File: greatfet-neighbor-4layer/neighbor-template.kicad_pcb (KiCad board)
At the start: 4 copper layers, 70.7 x 53.3 mm, 13 parts, among them J1 NEIGHBOR1, J2 NEIGHBOR2, J7 BONUS_ROW, U1 M24C02-FMN6TP

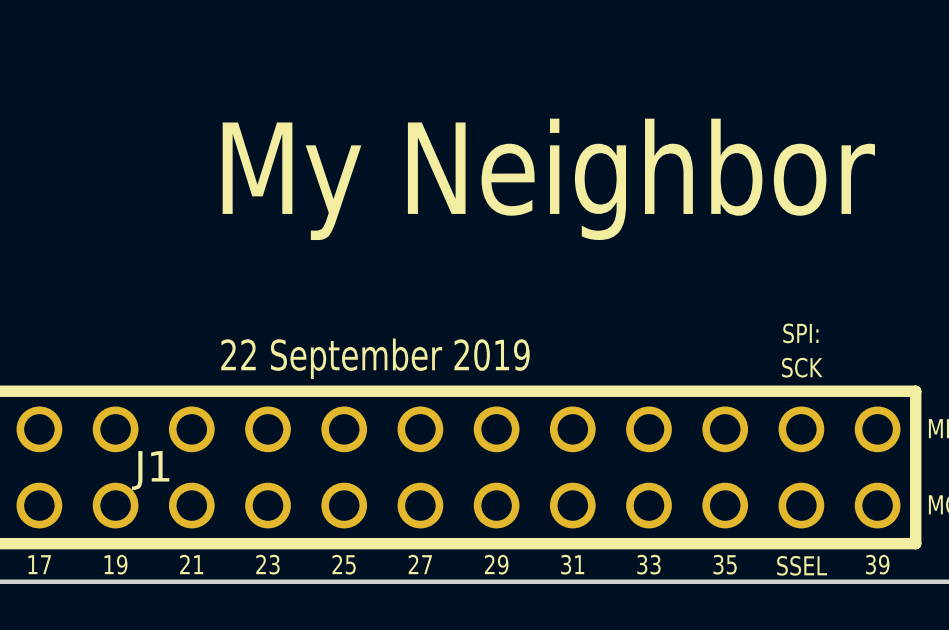
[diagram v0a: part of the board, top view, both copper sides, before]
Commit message: add "for GreatFET" to schematic, silkscreen add template README
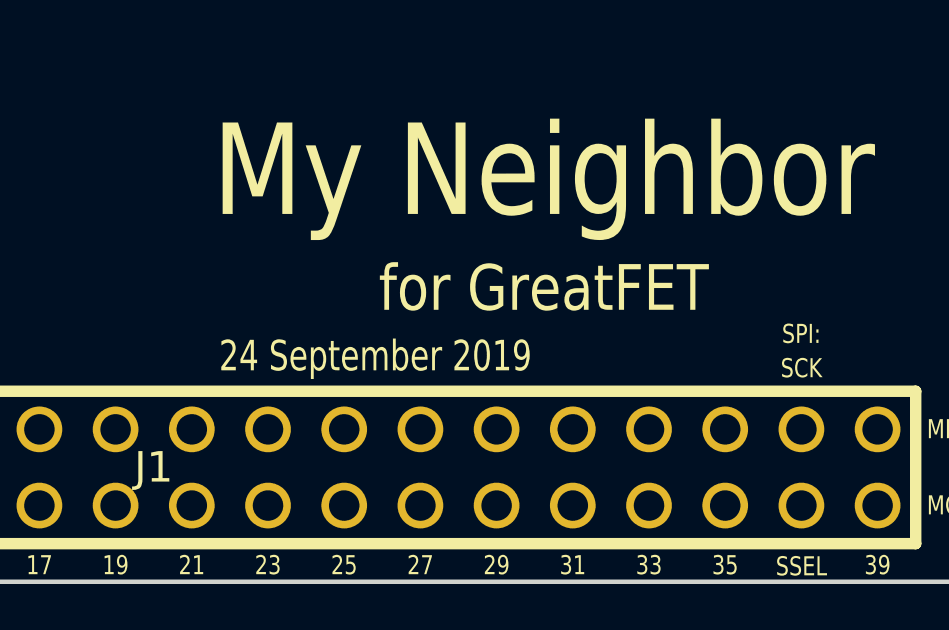
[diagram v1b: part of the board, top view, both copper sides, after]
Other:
- board text added: "24 September 2019"
- board text added: "for GreatFET"
- board text removed: "22 September 2019"
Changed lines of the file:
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@@
   (general
     (thickness 1.6)
-    (drawings 236)
+    (drawings 237)
     (tracks 64)
     (zones 0)
@@
       (net 1 GND))
   )
+  (gr_text "for GreatFET" (at 159.05 112.15) (layer F.SilkS)
+    (effects (font (size 1.524 1.27) (thickness 0.2286)))
+  )
   (gr_line (start 109.6772 98.933) (end 109.728 99.9998) (angle 90) (layer Edge.Cuts) (width 0.15))
   (gr_line (start 109.6264 97.4852) (end 109.6772 98.933) (angle 90) (layer Edge.Cuts) (width 0.15))
@@
   (gr_line (start 177.9016 92.3544) (end 177.8508 94.0054) (angle 90) (layer Edge.Cuts) (width 0.15))
   (gr_line (start 177.9524 90.5002) (end 177.9016 92.3544) (angle 90) (layer Edge.Cuts) (width 0.15))
-  (gr_text "22 September 2019" (at 153.4414 114.4016) (layer F.SilkS)
+  (gr_text "24 September 2019" (at 153.4414 114.4016) (layer F.SilkS)
     (effects (font (size 1.016 0.762) (thickness 0.1524)))
   )

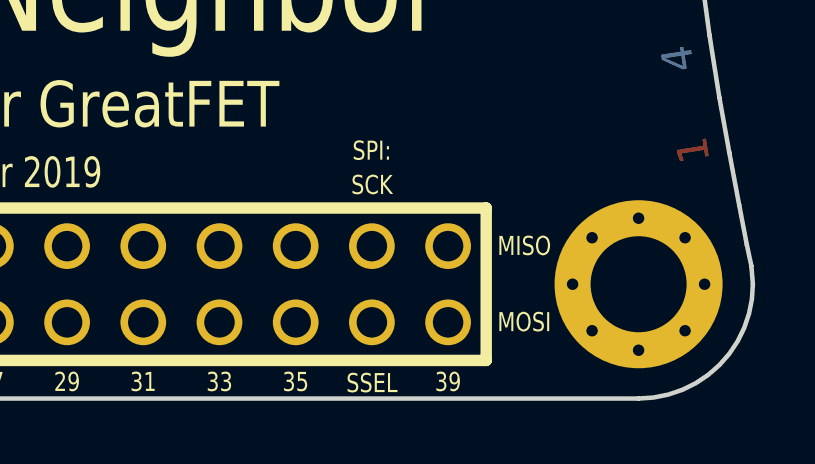
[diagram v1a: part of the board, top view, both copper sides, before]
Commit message: adopt OSHWA convention for SPI signal names https://www.oshwa.org/a-resolution-to-redefine-spi-signal-names
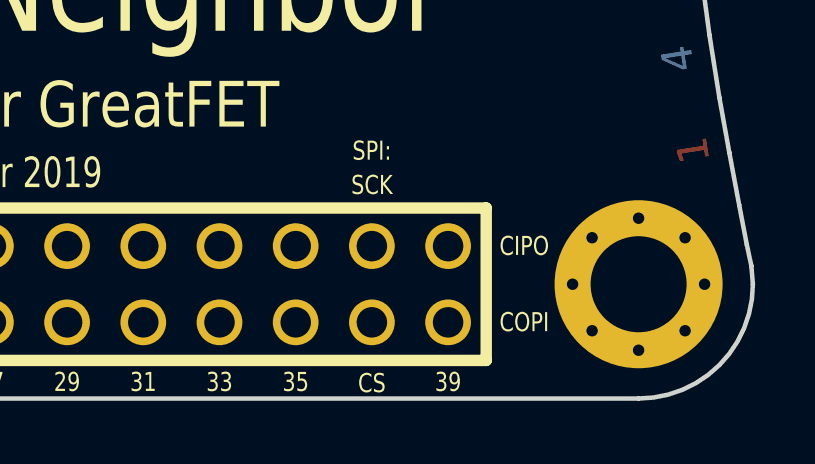
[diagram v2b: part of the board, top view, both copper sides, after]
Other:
- board text added: "CIPO"
- board text added: "COPI"
- board text added: "CS"
- board text removed: "MISO"
- board text removed: "MOSI"
- board text removed: "SSEL"
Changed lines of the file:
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@@
     (effects (font (size 0.635 0.508) (thickness 0.1016)) (justify mirror))
   )
-  (gr_text MOSI (at 172.72 119.38) (layer B.SilkS)
-    (effects (font (size 0.635 0.508) (thickness 0.1016)) (justify mirror))
-  )
-  (gr_text MISO (at 172.72 116.84) (layer B.SilkS)
+  (gr_text COPI (at 172.72 119.38) (layer B.SilkS)
+    (effects (font (size 0.635 0.508) (thickness 0.1016)) (justify mirror))
+  )
+  (gr_text CIPO (at 172.72 116.84) (layer B.SilkS)
     (effects (font (size 0.635 0.508) (thickness 0.1016)) (justify mirror))
   )
@@
     (effects (font (size 0.635 0.508) (thickness 0.1016)) (justify mirror))
   )
-  (gr_text SSEL (at 167.64 121.412) (layer B.SilkS)
+  (gr_text CS (at 167.64 121.412) (layer B.SilkS)
     (effects (font (size 0.635 0.508) (thickness 0.1016)) (justify mirror))
   )
@@
     (effects (font (size 0.635 0.508) (thickness 0.1016)))
   )
-  (gr_text SSEL (at 167.64 121.412) (layer F.SilkS)
-    (effects (font (size 0.635 0.508) (thickness 0.1016)))
-  )
-  (gr_text MISO (at 172.72 116.84) (layer F.SilkS)
-    (effects (font (size 0.635 0.508) (thickness 0.1016)))
-  )
-  (gr_text MOSI (at 172.72 119.38) (layer F.SilkS)
-    (effects (font (size 0.635 0.508) (thickness 0.1016)))
-  )
+  (gr_text CS (at 167.64 121.412) (layer F.SilkS)
+    (effects (font (size 0.635 0.508) (thickness 0.1016)))
+  )
+  (gr_text CIPO (at 172.72 116.84) (layer F.SilkS)
+    (effects (font (size 0.635 0.508) (thickness 0.1016)))
+  )
+  (gr_text COPI (at 172.72 119.38) (layer F.SilkS)
+    (effects (font (size 0.635 0.508) (thickness 0.1016)))
+  )
